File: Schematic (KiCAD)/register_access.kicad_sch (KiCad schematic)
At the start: 158 parts, among them J4 NAND_7, J5 NAND_7, J6 NOR_2, J7 INVERT, J8 NOR_2, K10 NAND_2, K11 NAND_4, K12 NOR_2, K13 NAND_2, K14 NAND_4, K15 NOR_2, K16 NAND_2, K17 NAND_4, K19 NAND_4, K20 NAND_4, K21 NAND_4, K22 NAND_4, K26 NAND_4, K28 NAND_4, K29 NAND_4, K31 NAND_4, K32 NAND_4, K33 NAND_4, K35 NAND_4, K38 NAND_4, K40 NAND_4, K41 NAND_4, K42 NAND_4, K43 NAND_4, K45 NAND_4, K46 NAND_4, K49 NAND_4, K50 NAND_4, K52 NAND_4, K54 NAND_4, K56 NAND_4, K58 NAND_4, K60 NAND_4, K64 NAND_4, K65 NAND_4, K66 NAND_4, K67 NAND_4, K69 NAND_4, K71 NAND_4, K72 NOR_2, K73 NAND_2, K75 NAND_4, K76 NOR_2, K77 NAND_2, K78 NAND_4, K79 NOR_2, K8 NAND_4, K80 NAND_2, K81 NAND_4, K83 NAND_4, K85 NAND_4, K86 NAND_4, K87 NAND_4, K9 NOR_2, K91 NAND_4, K92 NAND_4, K93 NAND_4, K94 NAND_4, K95 NAND_2, K97 NAND_4

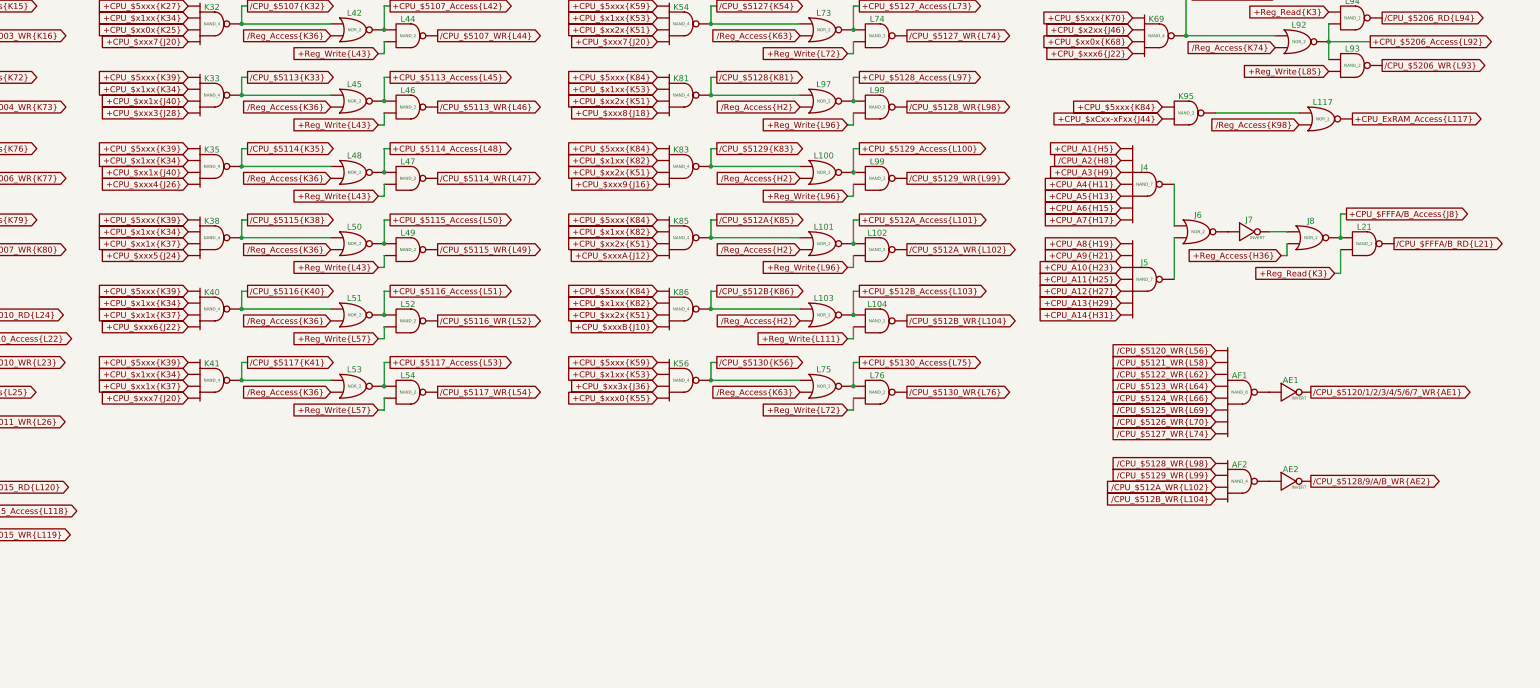
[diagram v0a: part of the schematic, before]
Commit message: Tracing and schematic updates.  - Added timer to schematic.  - Added all items from artifacts sheet to the MMC5A trace.
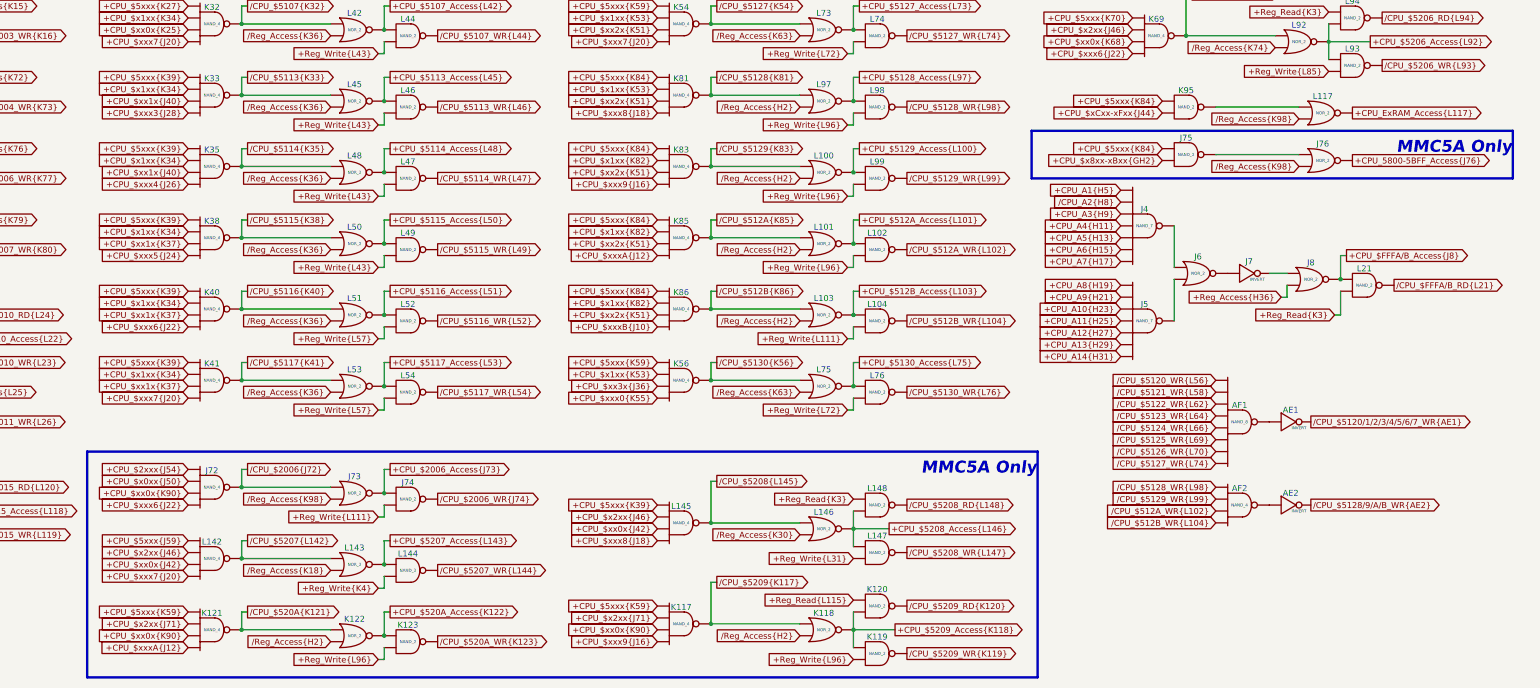
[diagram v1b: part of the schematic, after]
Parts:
- added J72, K117, K121, L142, L145: NAND_4, symbol MMC5:NAND_4
- added J73, J76, K118, K122, L143, L146: NOR_2, symbol MMC5:NOR_2
- added J74, J75, K119, K120, K123, L144, L147, L148: NAND_2, symbol MMC5:NAND_2
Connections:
- net +CPU_$2xxx{J54}: now also J72. (X)
- net +CPU_$5xxx{J59}: now also L142. (X)
- net +CPU_$5xxx{K39}: now also L145. (X)
- net +CPU_$5xxx{K59}: now also K117. (X), K121. (X)
- net +CPU_$5xxx{K84}: now also J75. (X)
- net +CPU_$x0xx{J50}: now also J72. (X)
- net +CPU_$x2xx{J46}: now also L142. (X), L145. (X)
- net +CPU_$xx0x{J42}: now also L142. (X), L145. (X)
- net +CPU_$xx0x{K90}: now also J72. (X), K117. (X), K121. (X)
- net +CPU_$xxx6{J22}: now also J72. (X)
- net +CPU_$xxx7{J20}: now also L142. (X)
- net +CPU_$xxx8{J18}: now also L145. (X)
- net +CPU_$xxx9{J16}: now also K117. (X)
- net +CPU_$xxxA{J12}: now also K121. (X)
- net +Reg_Read{K3}: now also L148. (X)
- net +Reg_Read{L115}: now also K120. (X)
- net +Reg_Write{K4}: now also L144. (X)
- net +Reg_Write{L111}: now also J74. (X)
- net +Reg_Write{L31}: now also L147. (X)
- net +Reg_Write{L96}: now also K119. (X), K123. (X)
- net /Reg_Access{H2}: now also K118. (X), K122. (X)
- net /Reg_Access{K18}: now also L143. (X)
- net /Reg_Access{K30}: now also L146. (X)
- net /Reg_Access{K98}: now also J73. (X), J76. (X)
- net at J6. (X): now also J5. (X); no longer J4. (X)
- net at J7. (X): now also J8. (X); no longer J6. (X)
- new net: J4. (X), J6. (X)
- new net: J75. (X), J76. (X)
- new net: J6. (X), J7. (X)
- new net: AE2. (X), AF2. (X)
- new net: K95. (X), L117. (X)
- new net: AE1. (X), AF1. (X)
- new net +CPU_$2006_Access{J73}: J73. (X), J74. (X)
- new net +CPU_$5207_Access{L143}: L143. (X), L144. (X)
- new net +CPU_$5208_Access{L146}: L146. (X), L147. (X), L148. (X)
- new net +CPU_$5209_Access{K118}: K118. (X), K119. (X), K120. (X)
- new net +CPU_$520A_Access{K122}: K122. (X), K123. (X)
- new net +CPU_$x2xx{J71}: K117. (X), K121. (X)
- new net +CPU_$x8xx-xBxx{GH2}: J75. (X)
- new net +CPU_5800-5BFF_Access{J76}: J76. (X)
- new net /CPU_$2006_WR{J74}: J74. (X)
- new net /CPU_$2006{J72}: J72. (X), J73. (X)
- new net /CPU_$5207_WR{L144}: L144. (X)
- new net /CPU_$5207{L142}: L142. (X), L143. (X)
- new net /CPU_$5208_RD{L148}: L148. (X)
- new net /CPU_$5208_WR{L147}: L147. (X)
- new net /CPU_$5208{L145}: L145. (X), L146. (X)
- new net /CPU_$5209_RD{K120}: K120. (X)
- new net /CPU_$5209_WR{K119}: K119. (X)
- new net /CPU_$5209{K117}: K117. (X), K118. (X)
- new net /CPU_$520A_WR{K123}: K123. (X)
- new net /CPU_$520A{K121}: K121. (X), K122. (X)
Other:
- note added: "MMC5A Only"
- moved on the sheet: AE1, AE2, AF1, AF2, J4, J5, J6, J7, J8, K95, L117, L21

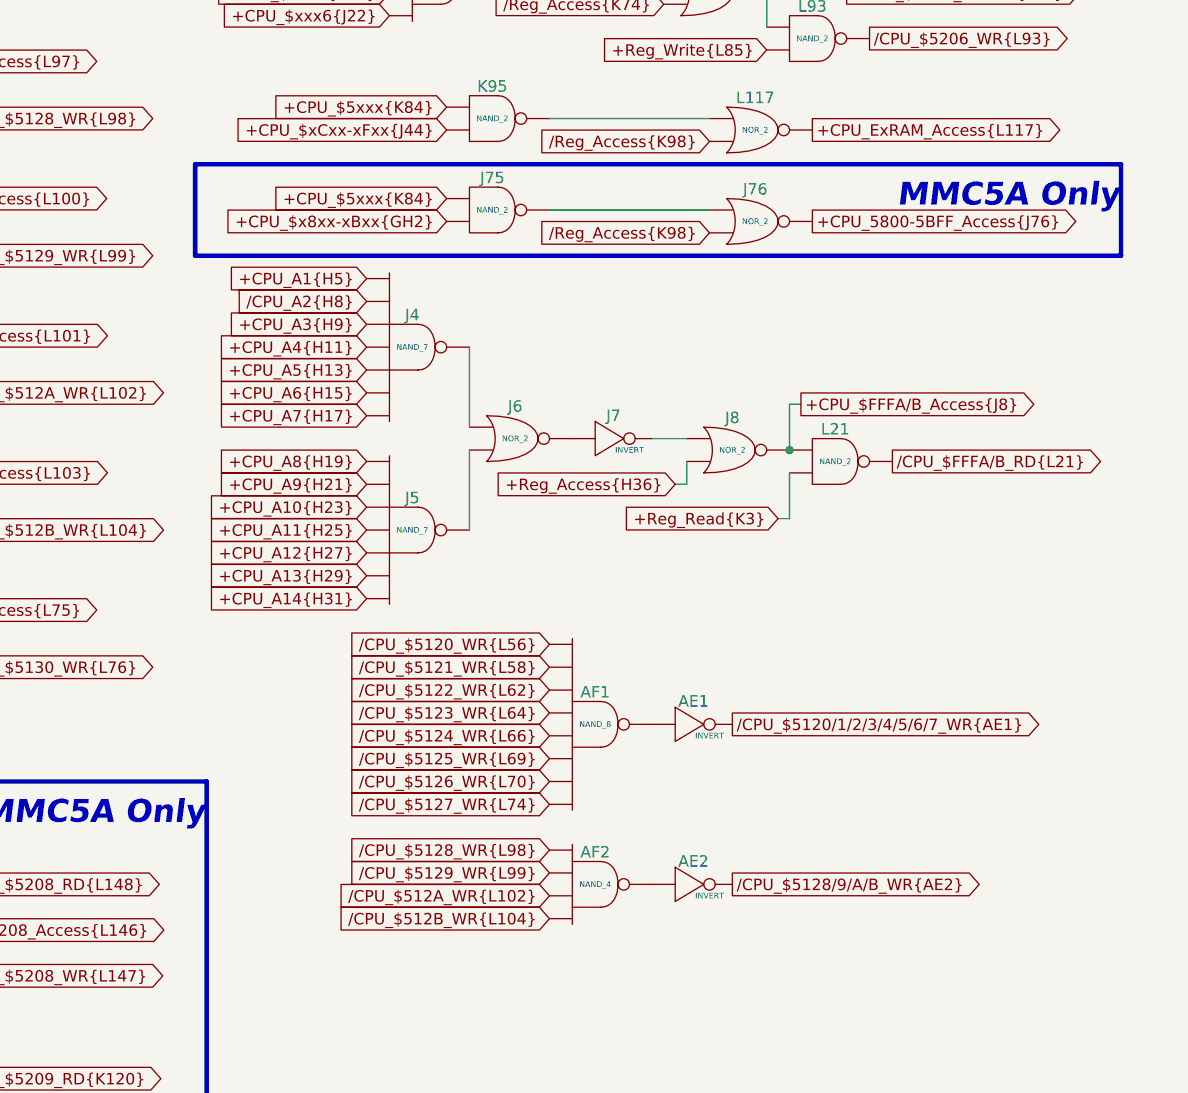
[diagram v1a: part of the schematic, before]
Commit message: - Updated all of the various And-OR-Invert gates to have consistent names.  - Added the schematic for CL3 / SL3 GPIO pins.  There are no surprises revealed by this.  - Finished up the CPU address decoding tracing.  - Added one of the 'artifact' counters from the pulse channels
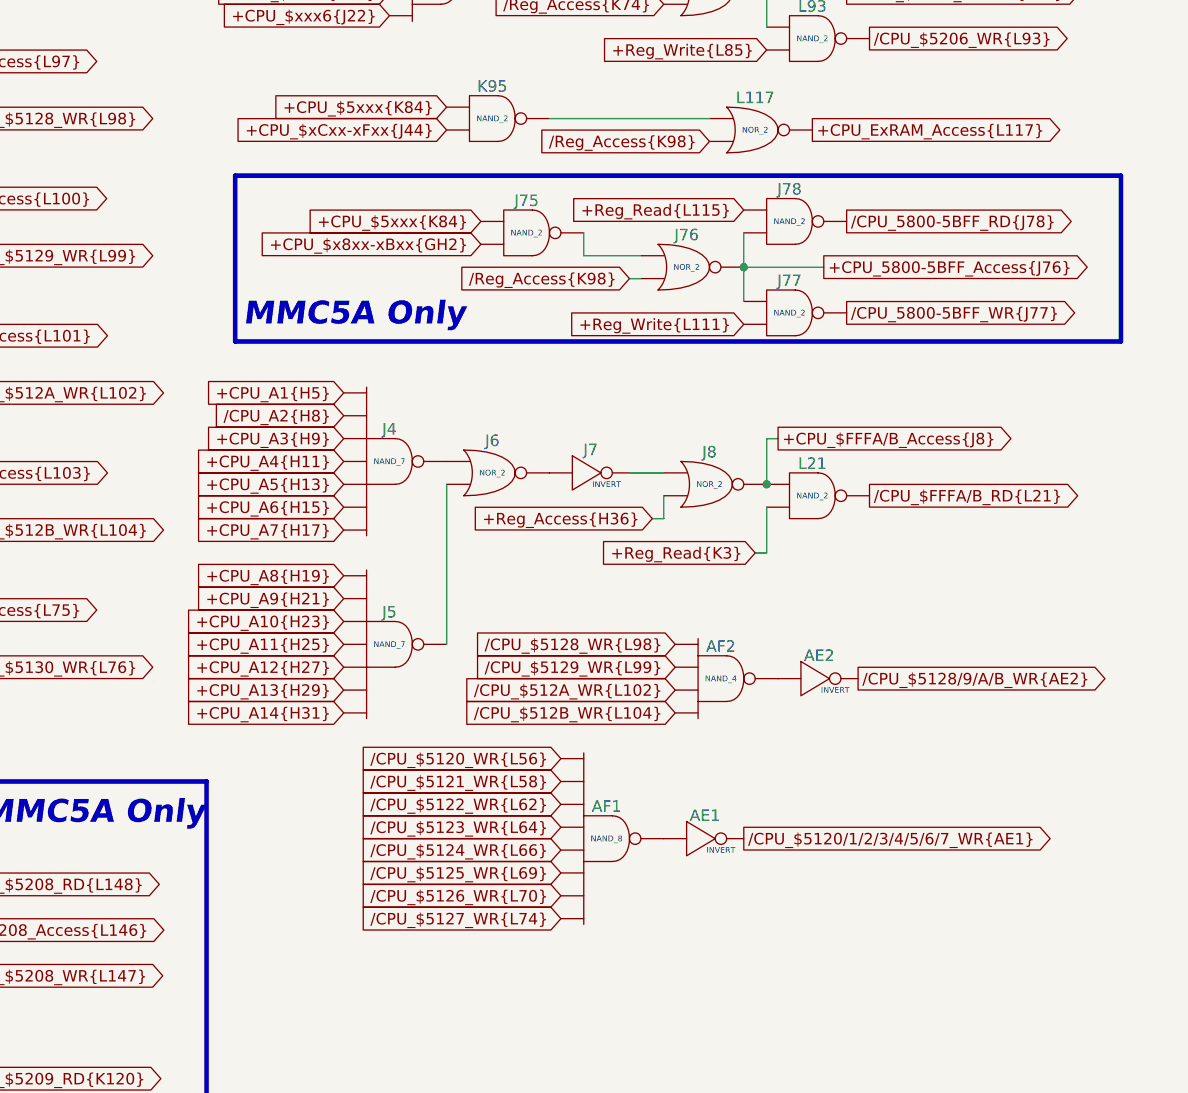
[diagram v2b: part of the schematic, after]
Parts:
- added J77, J78: NAND_2, symbol MMC5:NAND_2
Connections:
- net +CPU_5800-5BFF_Access{J76}: now also J77. (X), J78. (X)
- net +Reg_Read{L115}: now also J78. (X)
- net +Reg_Write{L111}: now also J77. (X)
- net at J6. (X): now also J5. (X); no longer J4. (X)
- net at J7. (X): now also J8. (X); no longer J6. (X)
- new net: J4. (X), J6. (X)
- new net: J75. (X), J76. (X)
- new net: J6. (X), J7. (X)
- new net: AE2. (X), AF2. (X)
- new net: K95. (X), L117. (X)
- new net: AE1. (X), AF1. (X)
- new net /CPU_5800-5BFF_RD{J78}: J78. (X)
- new net /CPU_5800-5BFF_WR{J77}: J77. (X)
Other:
- moved on the sheet: AE1, AE2, AF1, AF2, J4, J5, J6, J7, J75, J76, J8, L21
